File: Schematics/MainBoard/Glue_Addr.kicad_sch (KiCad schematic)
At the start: 26 parts, among them IC1 ATF1508AS-7AX100, J1 Conn_02x05_Odd_Even, X1 16MHz

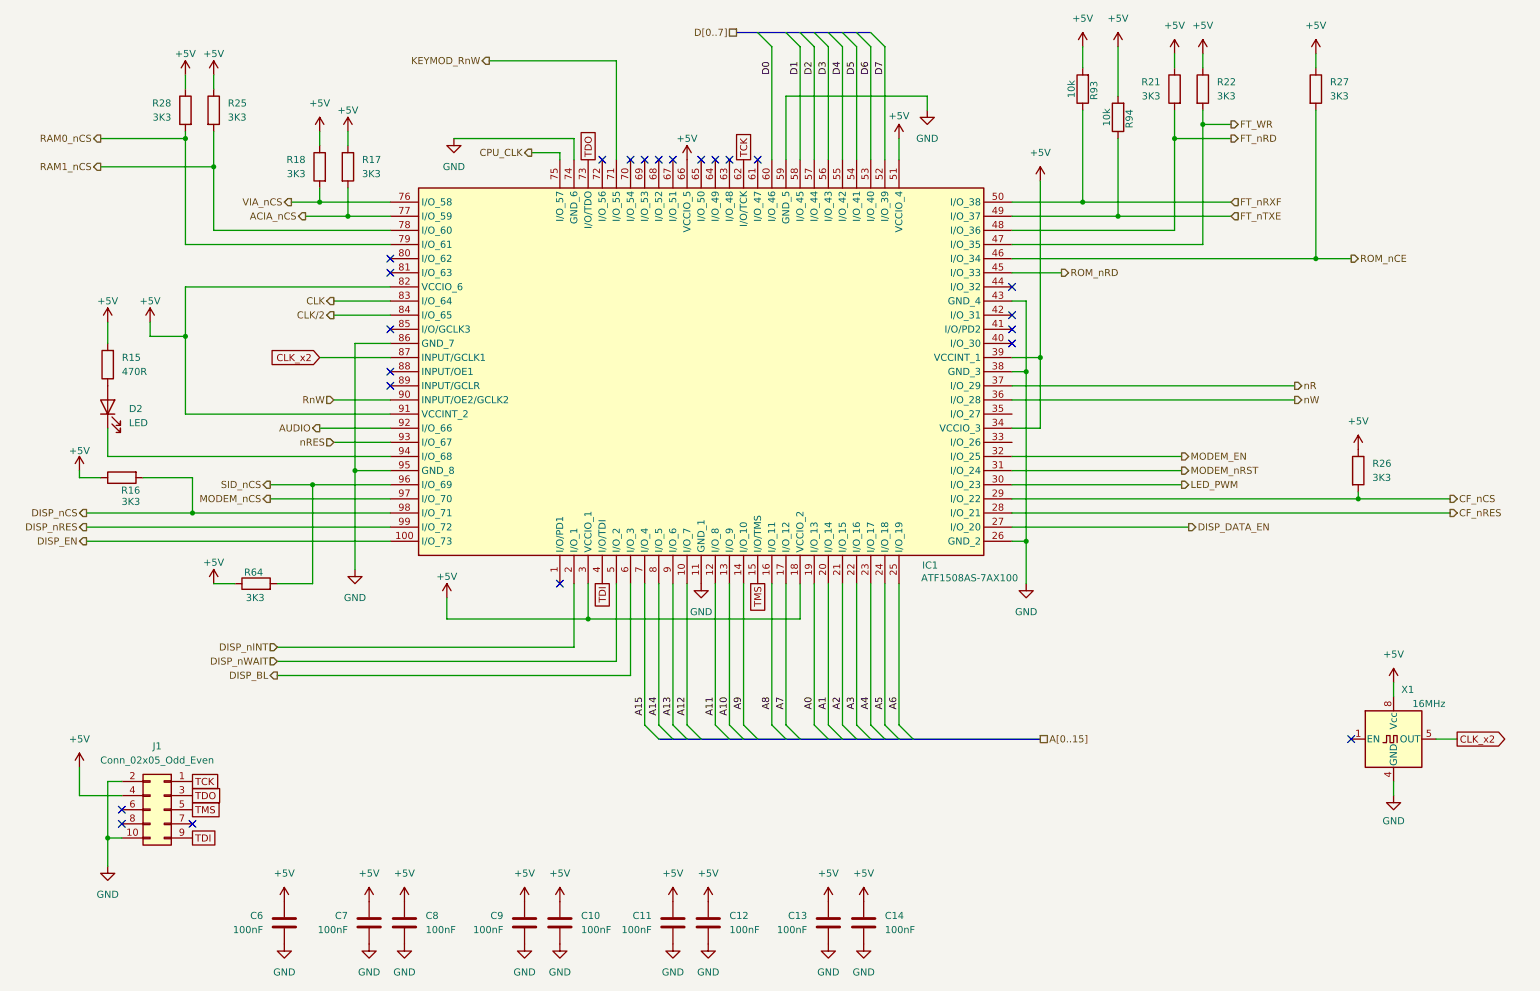
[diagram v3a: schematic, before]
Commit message: Completed routing
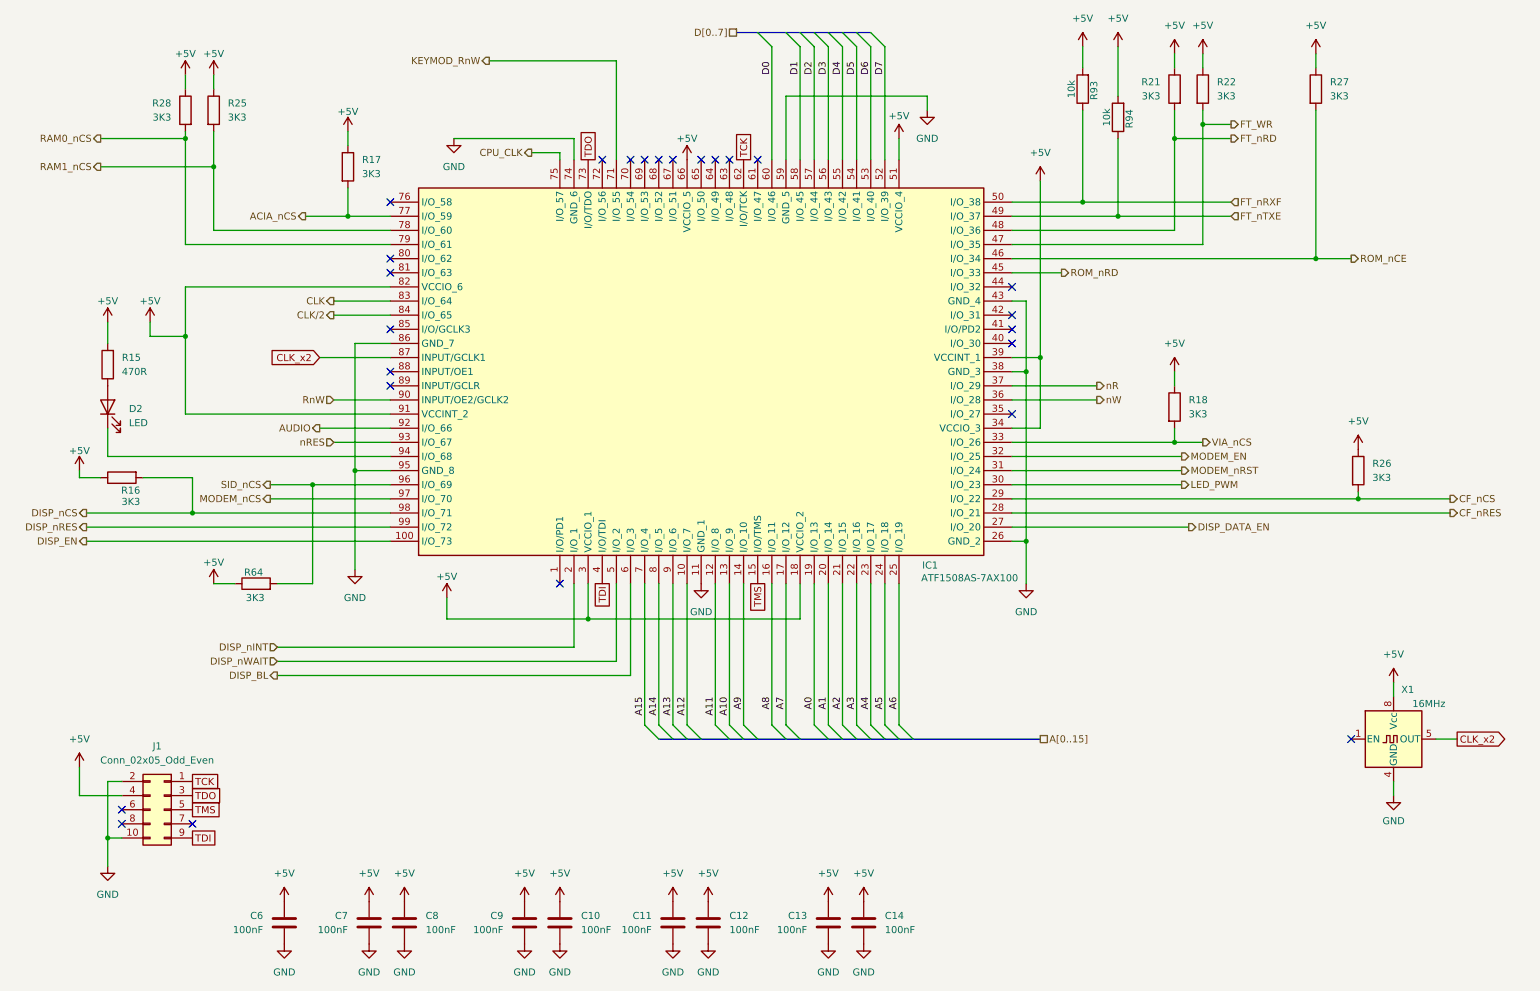
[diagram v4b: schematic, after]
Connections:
- net VIA_nCS: now also IC1.33 (I/O_26); no longer IC1.76 (I/O_58)
- no-connect marks 23 -> 25
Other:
- moved on the sheet: R18
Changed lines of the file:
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@@
 	)
 	(junction
-		(at 68.58 53.34)
+		(at 222.25 96.52)
 		(diameter 0)
 		(color 0 0 0 0)
@@
 	)
 	(no_connect
+		(at 81.28 53.34)
+	)
+	(no_connect
 		(at 147.32 45.72)
 	)
@@
 	)
 	(no_connect
+		(at 193.04 91.44)
+	)
+	(no_connect
 		(at 193.04 68.58)
 	)
@@
 	(wire
 		(pts
-			(xy 63.5 53.34) (xy 68.58 53.34)
+			(xy 227.33 96.52) (xy 222.25 96.52)
 		)
 		(stroke
@@
 	(wire
 		(pts
-			(xy 68.58 53.34) (xy 81.28 53.34)
+			(xy 195.58 71.12) (xy 193.04 71.12)
 		)
 		(stroke
@@
 	(wire
 		(pts
-			(xy 195.58 71.12) (xy 193.04 71.12)
+			(xy 92.71 41.91) (xy 114.3 41.91)
 		)
 		(stroke
@@
 	(wire
 		(pts
-			(xy 92.71 41.91) (xy 114.3 41.91)
+			(xy 73.66 50.8) (xy 73.66 55.88)
 		)
 		(stroke
@@
 	(wire
 		(pts
-			(xy 73.66 50.8) (xy 73.66 55.88)
+			(xy 222.25 26.67) (xy 222.25 29.21)
 		)
 		(stroke
@@
 	(wire
 		(pts
-			(xy 222.25 26.67) (xy 222.25 29.21)
+			(xy 193.04 96.52) (xy 222.25 96.52)
 		)
 		(stroke
@@
 	(wire
 		(pts
-			(xy 243.84 88.9) (xy 193.04 88.9)
+			(xy 208.28 88.9) (xy 193.04 88.9)
 		)
 		(stroke
@@
 	(wire
 		(pts
-			(xy 68.58 50.8) (xy 68.58 53.34)
+			(xy 222.25 93.98) (xy 222.25 96.52)
 		)
 		(stroke
@@
 	(wire
 		(pts
-			(xy 243.84 86.36) (xy 193.04 86.36)
+			(xy 208.28 86.36) (xy 193.04 86.36)
 		)
 		(stroke
@@
 	(wire
 		(pts
-			(xy 68.58 40.64) (xy 68.58 43.18)
+			(xy 222.25 83.82) (xy 222.25 86.36)
 		)
 		(stroke
@@
 	(hierarchical_label "VIA_nCS"
 		(shape output)
-		(at 63.5 53.34 180)
+		(at 227.33 96.52 0)
 		(effects
 			(font
 				(size 1.27 1.27)
 			)
-			(justify right)
+			(justify left)
 		)
 	)
@@
 	(hierarchical_label "nW"
 		(shape output)
-		(at 243.84 88.9 0)
+		(at 208.28 88.9 0)
 		(effects
 			(font
@@
 	(hierarchical_label "nR"
 		(shape output)
-		(at 243.84 86.36 0)
+		(at 208.28 86.36 0)
 		(effects
 			(font
@@
 		)
 		(property "Value" "+5V"
-			(at 73.66 36.83 0)
+			(at 73.66 37.084 0)
 			(effects
 				(font
@@
 	(symbol
 		(lib_id "power:+5V")
-		(at 68.58 40.64 0)
-		(mirror y)
+		(at 222.25 83.82 0)
 		(unit 1)
 		(exclude_from_sim no)
@@
 		(fields_autoplaced yes)
 		(property "Reference" "#PWR066"
-			(at 68.58 44.45 0)
+			(at 222.25 87.63 0)
 			(effects
 				(font
@@
 		)
 		(property "Value" "+5V"
-			(at 68.58 35.56 0)
+			(at 222.25 78.74 0)
 			(effects
 				(font
@@
 		)
 		(property "Footprint" ""
-			(at 68.58 40.64 0)
+			(at 222.25 83.82 0)
 			(effects
 				(font
@@
 		)
 		(property "Datasheet" ""
-			(at 68.58 40.64 0)
+			(at 222.25 83.82 0)
 			(effects
 				(font
@@
 		)
 		(property "Description" ""
-			(at 68.58 40.64 0)
+			(at 222.25 83.82 0)
 			(effects
 				(font
@@
 	(symbol
 		(lib_id "Device:R")
-		(at 68.58 46.99 0)
-		(mirror y)
+		(at 222.25 90.17 0)
 		(unit 1)
 		(exclude_from_sim no)
@@
 		(fields_autoplaced yes)
 		(property "Reference" "R18"
-			(at 66.04 45.7199 0)
+			(at 224.79 88.8999 0)
 			(effects
 				(font
@@
 		)
 		(property "Value" "3K3"
-			(at 66.04 48.2599 0)
+			(at 224.79 91.4399 0)
 			(effects
 				(font
@@
 		)
 		(property "Footprint" "Resistor_SMD:R_0402_1005Metric"
-			(at 70.358 46.99 90)
+			(at 220.472 90.17 90)
 			(effects
 				(font
@@
 		)
 		(property "Datasheet" "~"
-			(at 68.58 46.99 0)
+			(at 222.25 90.17 0)
 			(effects
 				(font
@@
 		)
 		(property "Description" ""
-			(at 68.58 46.99 0)
+			(at 222.25 90.17 0)
 			(effects
 				(font
@@
 		)
 		(property "LCSC" "C25890"
-			(at 68.58 46.99 0)
+			(at 222.25 90.17 0)
 			(effects
 				(font

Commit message: Updates based on production files for JLC
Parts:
- C10: LCSC C1581 -> C307331
- C11, C12, C13, C14, C6, C7, C8, C9: LCSC C113803 -> C307331
- D2: LCSC DNF -> C2286
- IC1, J1: now not fitted
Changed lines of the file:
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@@
 			)
 		)
-		(property "LCSC" "C113803"
+		(property "LCSC" "C307331"
 			(at 138.43 182.88 0)
 			(effects
@@
 			)
 		)
-		(property "LCSC" "DNF"
+		(property "LCSC" "C2286"
 			(at 30.48 90.17 90)
 			(effects
@@
 		(in_bom yes)
 		(on_board yes)
-		(dnp no)
+		(dnp yes)
 		(property "Reference" "IC1"
 			(at 178.308 118.618 90)
@@
 		(in_bom yes)
 		(on_board yes)
-		(dnp no)
+		(dnp yes)
 		(fields_autoplaced yes)
 		(property "Reference" "J1"
@@
 			)
 		)
-		(property "LCSC" "C113803"
+		(property "LCSC" "C307331"
 			(at 132.08 182.88 0)
 			(effects
@@
 			)
 		)
-		(property "LCSC" "C113803"
+		(property "LCSC" "C307331"
 			(at 160.02 182.88 0)
 			(effects
@@
 			)
 		)
-		(property "LCSC" "C113803"
+		(property "LCSC" "C307331"
 			(at 105.41 182.88 0)
 			(effects
@@
 			)
 		)
-		(property "LCSC" "C1581"
+		(property "LCSC" "C307331"
 			(at 111.76 182.88 0)
 			(effects
@@
 			)
 		)
-		(property "LCSC" "C113803"
+		(property "LCSC" "C307331"
 			(at 77.47 182.88 0)
 			(effects
@@
 			)
 		)
-		(property "LCSC" "C113803"
+		(property "LCSC" "C307331"
 			(at 62.23 182.88 0)
 			(effects
@@
 			)
 		)
-		(property "LCSC" "C113803"
+		(property "LCSC" "C307331"
 			(at 83.82 182.88 0)
 			(effects
@@
 			)
 		)
-		(property "LCSC" "C113803"
+		(property "LCSC" "C307331"
 			(at 166.37 182.88 0)
 			(effects

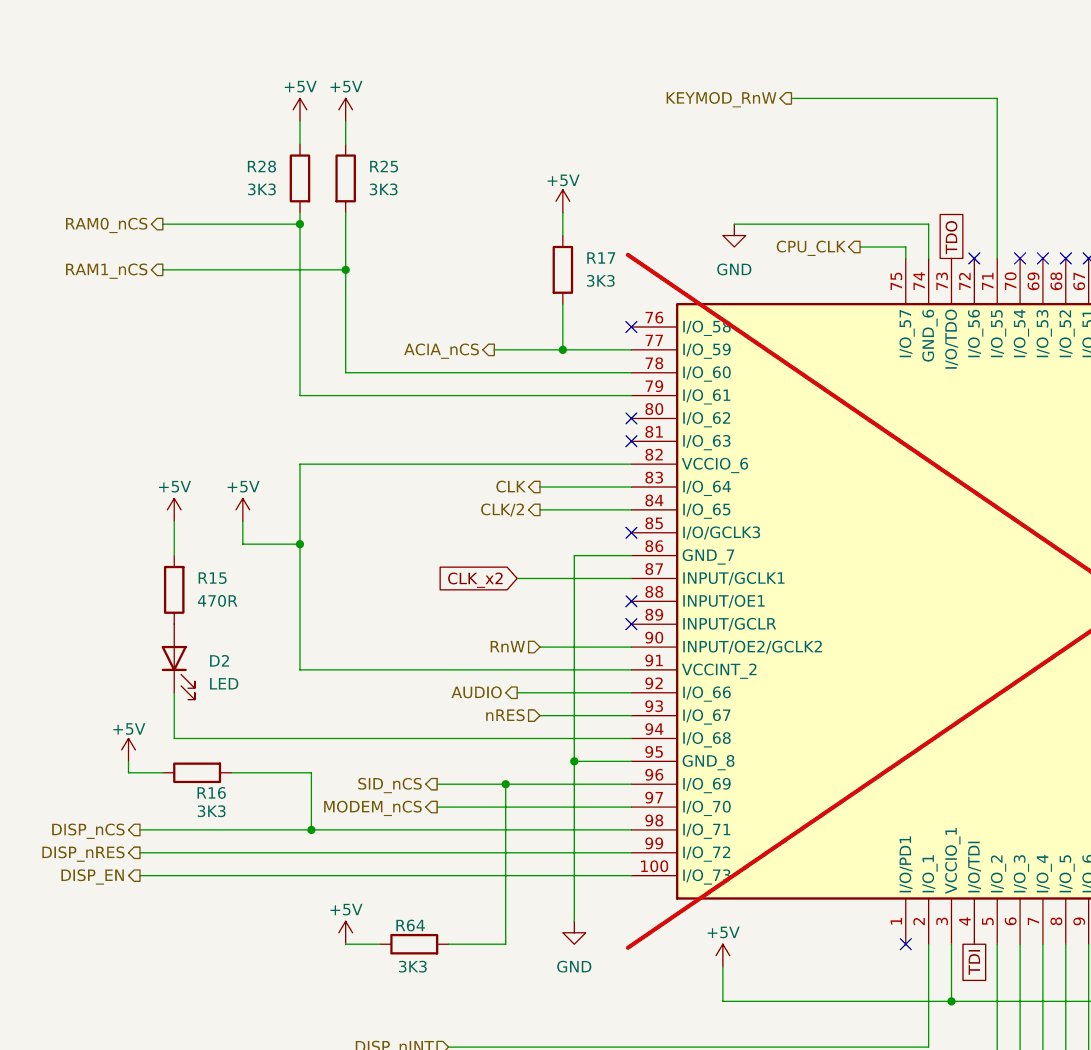
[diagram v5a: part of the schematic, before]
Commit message: Add some comments to schematic, update README, start on GLUE
Add some comments to schematic, update README, start on GLUE
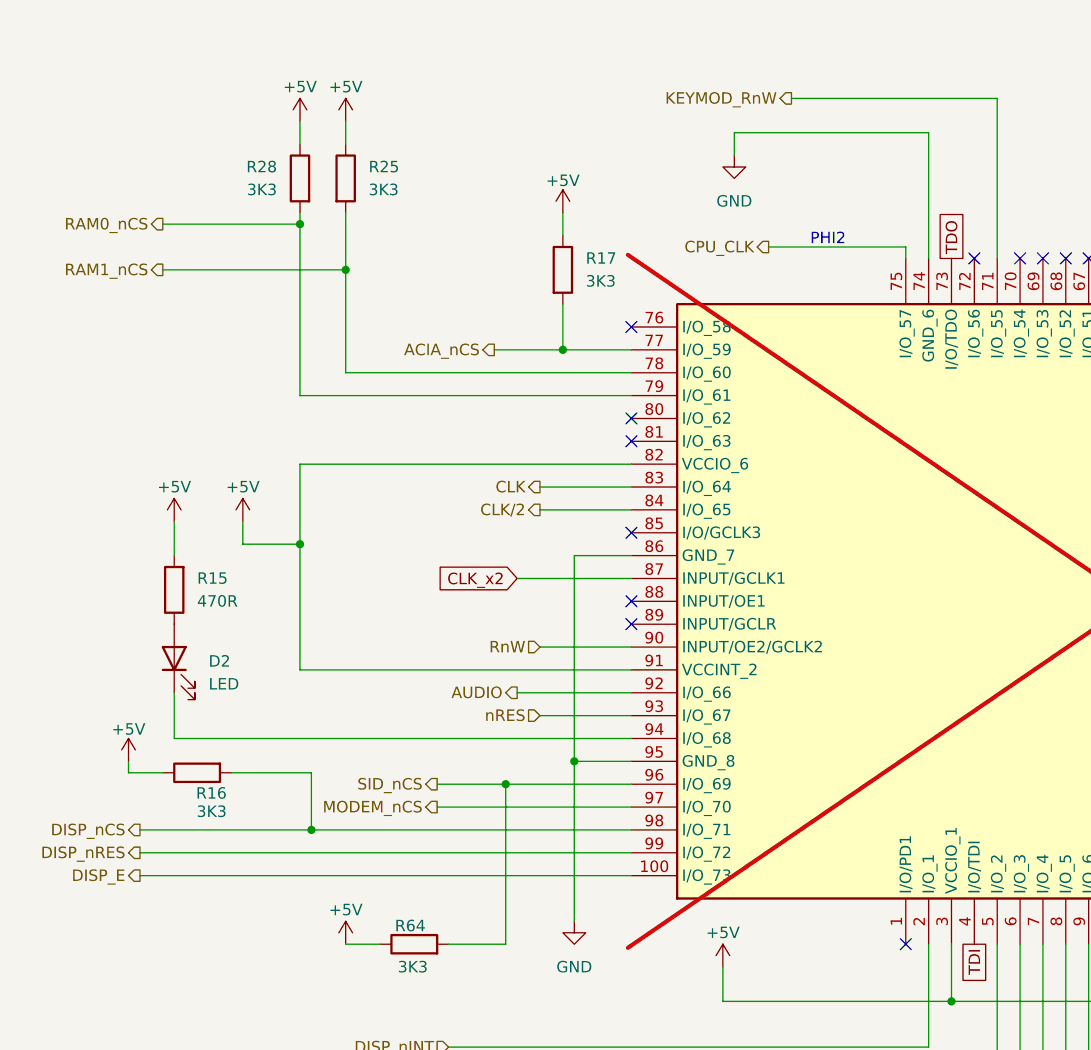
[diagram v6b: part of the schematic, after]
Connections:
- net DISP_EN renamed DISP_E
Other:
- note added: "PHI2"
